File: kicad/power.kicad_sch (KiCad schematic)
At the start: 54 parts, among them J4 TYPE-C-31-M-12, U10 MC34063AD, U11 MC34063AD, U12 XC6206P332MR-G, U13 TPS2116DRLR

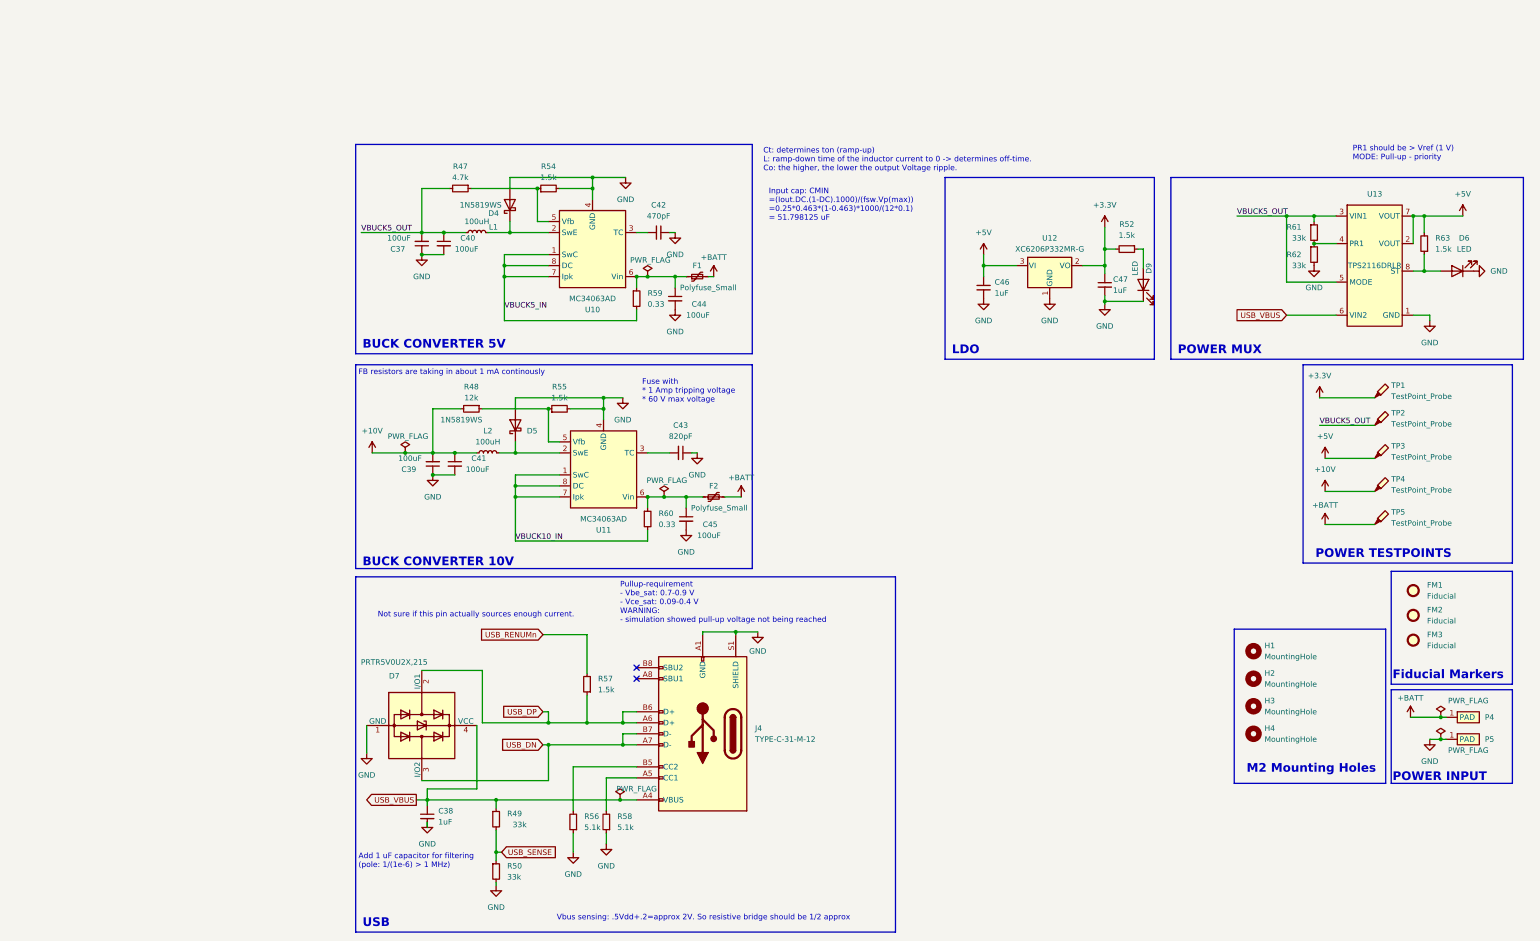
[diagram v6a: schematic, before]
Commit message: finished revision 1, generate gerbers and order
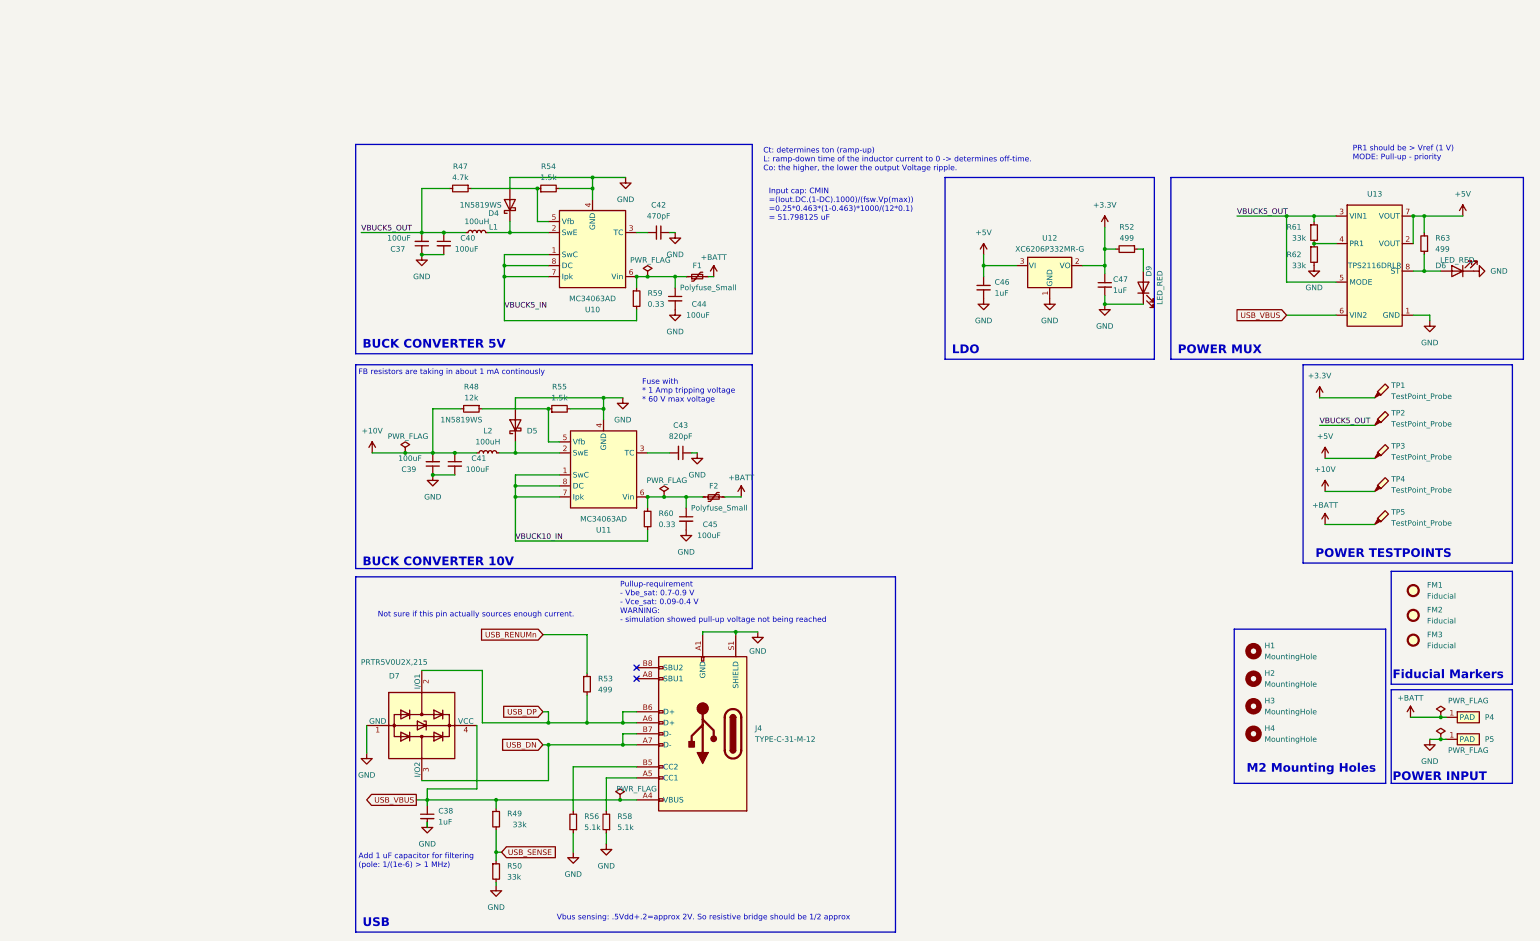
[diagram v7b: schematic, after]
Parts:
- removed R57: 1.5k, Resistor_SMD:R_0805_2012Metric, symbol Device:R_Small
- added R53: 499, Resistor_SMD:R_0402_1005Metric, symbol Device:R_Small
- D6, D9: value LED -> LED_RED; footprint LED_SMD:LED_0805_2012Metric -> LED_SMD:LED_0603_1608Metric; MFR.Part BZ-C0805-Y2-E1 -> F.0603.00139/P2-0603R1TS2-06T-002; jlcpcb C2833070 -> C7496820
- R52, R63: value 1.5k -> 499; footprint Resistor_SMD:R_0805_2012Metric -> Resistor_SMD:R_0402_1005Metric; MFR.Part 0805W8F1501T5E -> 0402WGF4990TCE; jlcpcb C4310 -> C4125
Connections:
- net USB_DP: now also R53.2
- net USB_RENUMn: now also R53.1
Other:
- moved on the sheet: D9
